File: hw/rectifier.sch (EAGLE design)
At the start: 0 parts

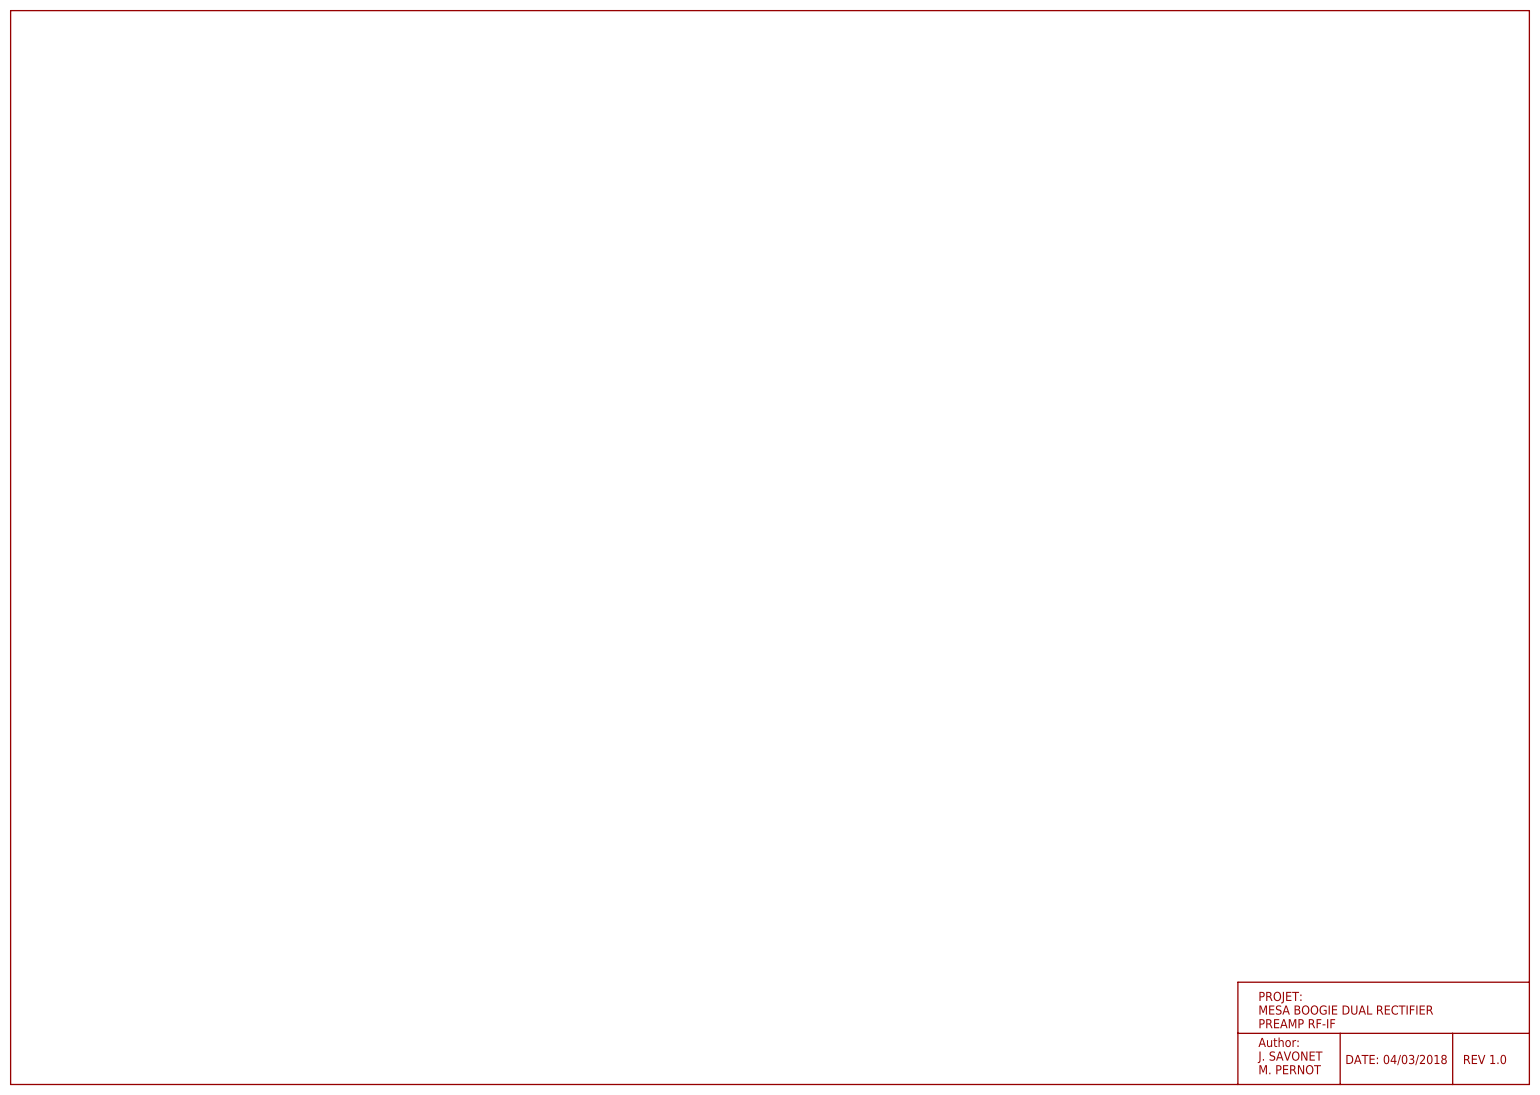
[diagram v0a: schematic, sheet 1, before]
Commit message: Add preamp
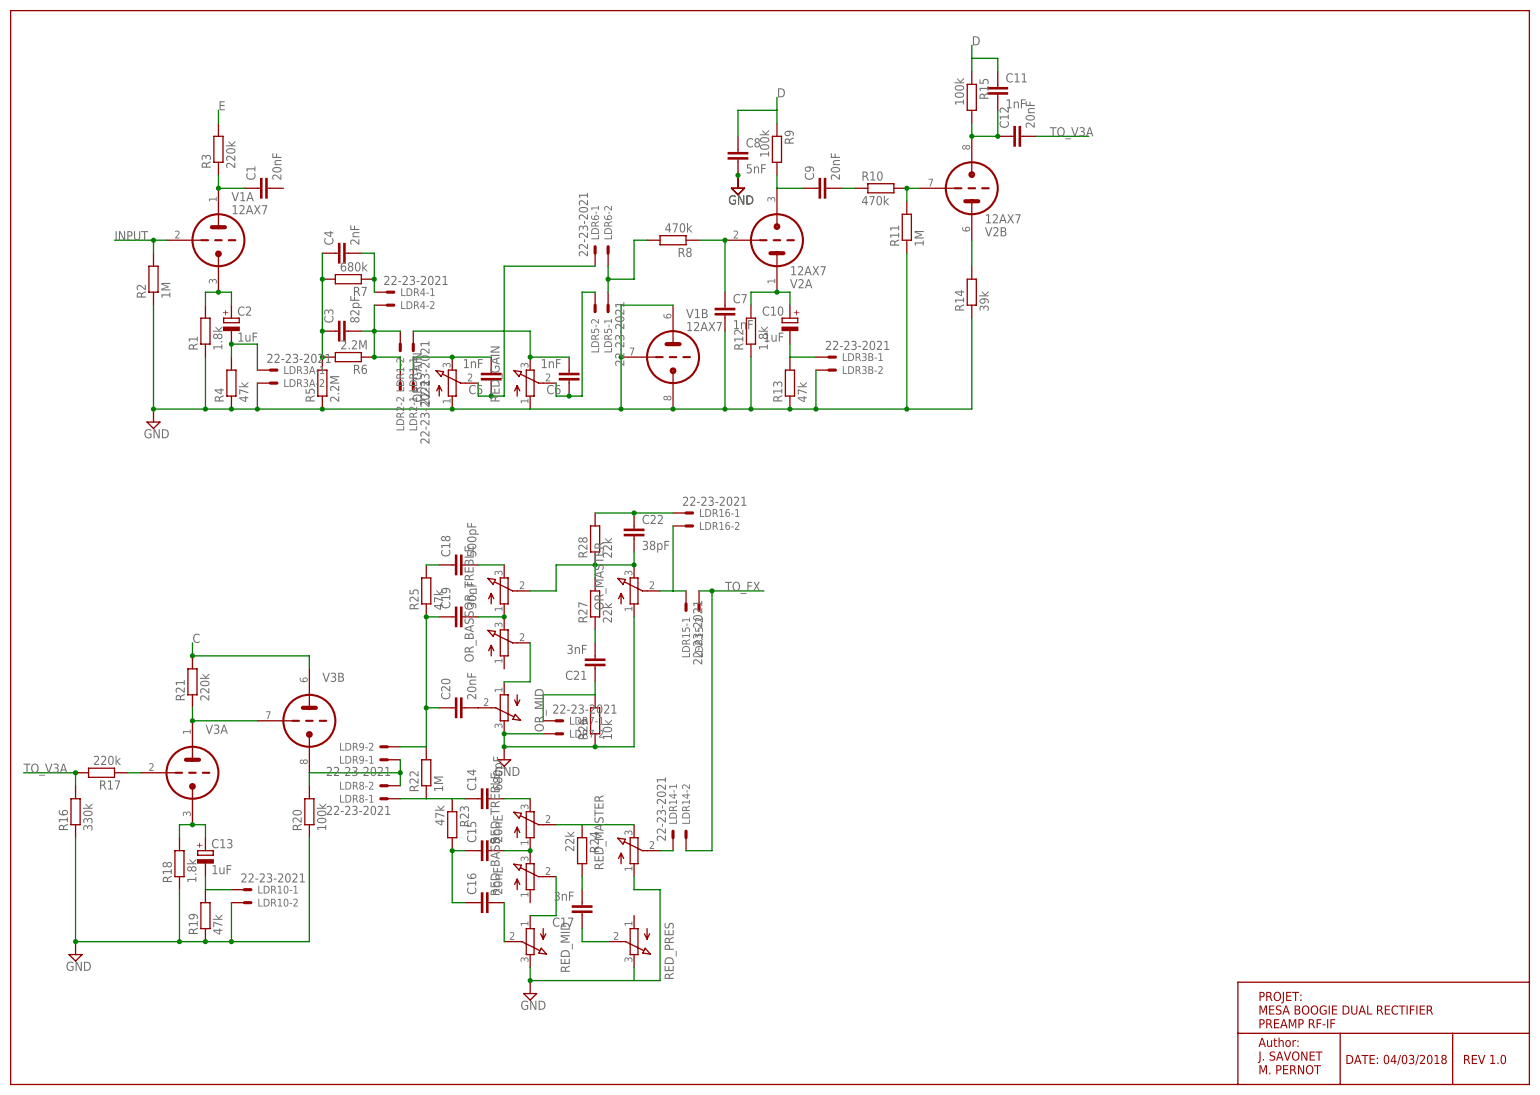
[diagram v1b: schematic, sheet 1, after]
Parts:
- added C1, C12, C15, C16, C20, C9: 20nF, capacitor-wima:C7.5/5
- added C10, C13, C2: 1uF, rcl:CPOL-EUE3.5-8
- added C11, C5, C6, C7: 1nF, capacitor-wima:C7.5/5
- added C14: 680pF, capacitor-wima:C7.5/5
- added C17, C21: 3nF, capacitor-wima:C7.5/5
- added C18: 500pF, capacitor-wima:C7.5/5
- added C19: 30nF, capacitor-wima:C7.5/5
- added C22: 38pF, capacitor-wima:C7.5/5
- added C3: 82pF, capacitor-wima:C7.5/5
- added C4: 2nF, capacitor-wima:C7.5/5
- added C8: 5nF, capacitor-wima:C7.5/5
- added LDR1, LDR10, LDR14, LDR15, LDR16, LDR2, LDR3A, LDR3B, LDR4, LDR5, LDR6, LDR7, LDR8, LDR9: 22-23-2021, con-molex:22-23-2021
- added OR_BASS, OR_GAIN, OR_MASTER, OR_MID, OR_TREBLE, RED_BASS, RED_GAIN, RED_MASTER, RED_MID, RED_PRES, RED_TREBLE: (no value), pot:3RP/1610N
- added R1, R12, R18: 1.8k, rcl:R-EU_0207/10
- added R10, R8: 470k, rcl:R-EU_0207/10
- added R11, R2, R22: 1M, rcl:R-EU_0207/10
- added R13, R19, R23, R25, R4: 47k, rcl:R-EU_0207/10
- added R14: 39k, rcl:R-EU_0207/10
- added R15, R20, R9: 100k, rcl:R-EU_0207/10
- added R16: 330k, rcl:R-EU_0207/10
- added R17, R21, R3: 220k, rcl:R-EU_0207/10
- added R24, R27, R28: 22k, rcl:R-EU_0207/10
- added R26: 10k, rcl:R-EU_0207/10
- added R5, R6: 2.2M, rcl:R-EU_0207/10
- added R7: 680k, rcl:R-EU_0207/10
- added V1, V2: 12AX7, tubes:12AX7-P
- added V3: (no value), tubes:12AX7-P
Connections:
- new net C: R21.2, V3B.TA
- new net D: C11.1, C8.1, R15.1, R9.1
- new net E: R3.2
- new net GND: C7.2, C8.2, LDR10-2.S, LDR3A-2.S, LDR3B-2.S, LDR7-2.S, OR_GAIN.A, OR_MASTER.A, OR_MID.E, R1.1, R11.1, R12.1, R13.1, R14.1, R16.1, R18.1, R19.1, R2.1, R20.1, R26.1, R4.1, R5.1, RED_GAIN.A, RED_MASTER.A, RED_MID.E, RED_PRES.E, V1B.TA, V1B.TG, V1B.TK
- new net INPUT: R2.2, V1A.TG
- new net LDR3_A: C2.-, LDR3A-1.S, R4.2
- new net LDR4_A: C4.2, LDR4-1.S, R7.1
- new net LDR4_B: C3.2, LDR1-2.S, LDR2-2.S, LDR4-2.S, R6.1
- new net N$1: C3.1, C4.1, R5.2, R6.2, R7.2
- new net N$10: C10.+, R12.2, V2A.TA
- new net N$11: C9.1, R9.2, V2A.TK
- new net N$12: R17.1, V3A.TG
- new net N$13: C10.-, LDR3B-1.S, R13.2
- new net N$14: C9.2, R10.1
- new net N$15: R10.2, R11.2, V2B.TG
- new net N$16: C13.+, R18.2, V3A.TK
- new net N$17: R14.2, V2B.TA
- new net N$18: C13.-, LDR10-1.S, R19.2
- new net N$19: C11.2, C12.1, R15.2, V2B.TK
- new net N$2: C2.+, R1.2, V1A.TK
- new net N$20: R21.1, V3A.TA, V3B.TG
- new net N$21: LDR8-2.S, LDR9-1.S, R20.2, V3B.TK
- new net N$22: C15.1, C16.1, R23.2
- new net N$23: C14.1, LDR8-1.S, R22.1, R23.1
- new net N$24: R24.1, RED_MASTER.E, RED_TREBLE.S
- new net N$25: C14.2, RED_TREBLE.E
- new net N$26: C15.2, RED_BASS.E, RED_TREBLE.A
- new net N$27: RED_BASS.S, RED_MID.A
- new net N$28: C16.2, RED_MID.S
- new net N$29: C19.1, C20.1, LDR9-2.S, R22.2, R25.1
- new net N$3: C1.1, R3.1, V1A.TA
- new net N$30: C17.2, R24.2
- new net N$31: C17.1, RED_PRES.S
- new net N$32: LDR14-1.S, RED_MASTER.S
- new net N$33: C18.1, R25.2
- new net N$34: C18.2, OR_TREBLE.E
- new net N$35: C19.2, OR_BASS.E, OR_TREBLE.A
- new net N$36: C20.2, OR_MID.S
- new net N$37: OR_BASS.S, OR_MID.A
- new net N$38: C21.1, LDR7-1.S, R26.2
- new net N$39: C21.2, R27.1
- new net N$4: LDR5-1.S, LDR6-2.S, R8.2
- new net N$40: C22.2, OR_MASTER.E, OR_TREBLE.S, R27.2, R28.1
- new net N$41: C22.1, LDR16-1.S, R28.2
- new net N$42: LDR15-1.S, LDR16-2.S, OR_MASTER.S
- new net N$5: C5.2, LDR2-1.S, OR_GAIN.E
- new net N$6: C5.1, LDR6-1.S, OR_GAIN.S
- new net N$7: C6.2, LDR1-1.S, RED_GAIN.E
- new net N$8: C6.1, LDR5-2.S, RED_GAIN.S
- new net N$9: C7.1, R8.1, V2A.TG
- new net TO_FX: LDR14-2.S, LDR15-2.S
- new net TO_V3A: C12.2, R16.2, R17.2

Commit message: Add loop section: wip
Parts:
- added C23, C28: 100nF, capacitor-wima:C7.5/5
- added C24: 47nF, capacitor-wima:C7.5/5
- added C27: 2u2, rcl:CPOL-EUE3.5-8
- added LDR3A1, LDR3A2, LDR3A3: 22-23-2021, con-molex:22-23-2021
- added LOOP_ACTIVE_MASTER, SEND_LEVEL: (no value), pot:3RP/1610N
- added R29, R30: 2M2, rcl:R-EU_0207/10
- added R31: 22k, rcl:R-EU_0207/10
- added R32: 82k, rcl:R-EU_0207/10
- added R33, R36: 1M, rcl:R-EU_0207/10
- added R34: 47k, rcl:R-EU_0207/10
- added R35: 2k2, rcl:R-EU_0207/10
- added R37: 120k, rcl:R-EU_0207/10
- added R38, R39: 3k3, rcl:R-EU_0207/10
- added V4: (no value), tubes:12AX7-P
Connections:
- new net N$43: C28.2, R29.1, R30.2, V4A.TG
- new net N$44: LDR3A1-2.S, LDR3A2-2.S, R34.2, V4B.TG
- new net N$45: R31.2, V4A.TK
- new net N$46: C23.1, R31.1, R32.2
- new net N$47: C23.2, LDR3A3-1.S, R33.2, R38.2, SEND_LEVEL.E
- new net N$48: C27.+, R35.2, V4B.TK
- new net N$49: C24.1, R37.1, V4B.TA
- new net N$50: LDR3A2-1.S, R38.1
- new net N$51: C24.2, LOOP_ACTIVE_MASTER.E
- new net N$52: LDR3A1-1.S, R39.1
- net C: now also R29.2, R37.2, V4A.TA
- net GND: now also C27.-, LOOP_ACTIVE_MASTER.A, R30.1, R32.1, R33.1, R34.1, R35.1, R36.1, SEND_LEVEL.A
- net TO_FX: now also C28.1, R36.2

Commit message: Start power section
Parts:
- added C26, C32, C33, C34: 30uF, rcl:CPOL-EUE3.5-8
- added C29: 047uF, capacitor-wima:C7.5/5
- added C30, C31: 220uF, rcl:CPOL-EUE3.5-8
- added D1, D2, D3, D4: 1N4004, diode:1N4004
- added L1: (no value), inductor-neosid:U15-CHOKE
- added LDR3: 22-23-2021, con-molex:22-23-2021
- added R41: 27k, rcl:R-EU_0207/10
- added R42, R43: 150k, rcl:R-EU_0207/10
- added R44: 2k7, rcl:R-EU_0207/10
- added R45: 15k, rcl:R-EU_0207/10
- added RECT_SELECT: 9077-2, switch-misc:9077-2
- added V5, V6: (no value), tubes:5U4GB
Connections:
- new net A: C29.2, L1.1, LDR3-2.S
- new net B: C26.+, L1.4, R44.1
- new net N$53: D1.C, D2.A
- new net N$54: D3.C, D4.A
- new net N$56: C30.-, C31.+, R42.2, R43.1
- new net N$57: V5.H1, V6.H1
- new net N$58: RECT_SELECT2.S, V5.A1, V6.A1
- new net N$59: RECT_SELECT1.S, V5.A2, V6.A2
- new net N$60: D3.A, RECT_SELECT2.O
- new net N$61: D1.A, RECT_SELECT1.O
- new net N$63: C30.+, D2.C, D4.C, LDR3-1.S, R42.1, V5.H2, V6.H2
- net C: now also C32.+, R41.2, R44.2, R45.2
- net D: now also C33.+, R45.1
- net E: now also C34.+, R41.1
- net GND: now also C26.-, C29.1, C31.-, C32.-, C33.-, C34.-, R43.2

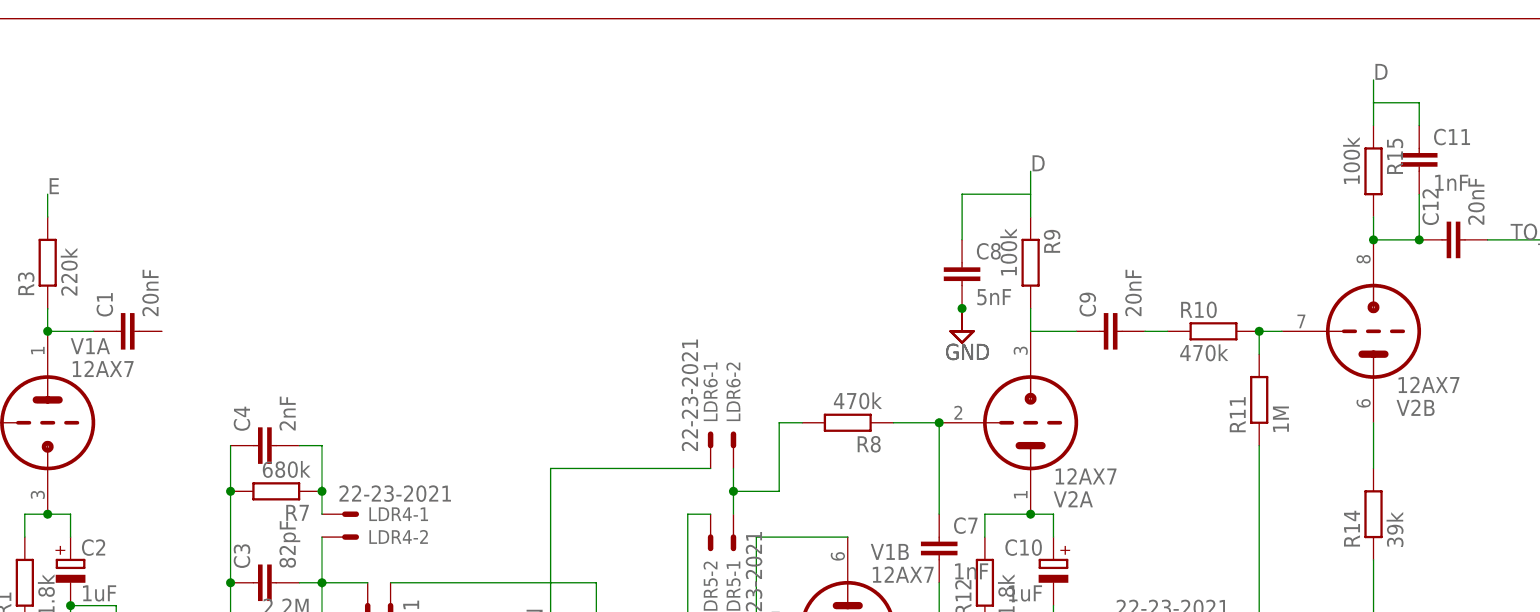
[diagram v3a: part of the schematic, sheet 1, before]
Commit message: Preamp: add missing wires
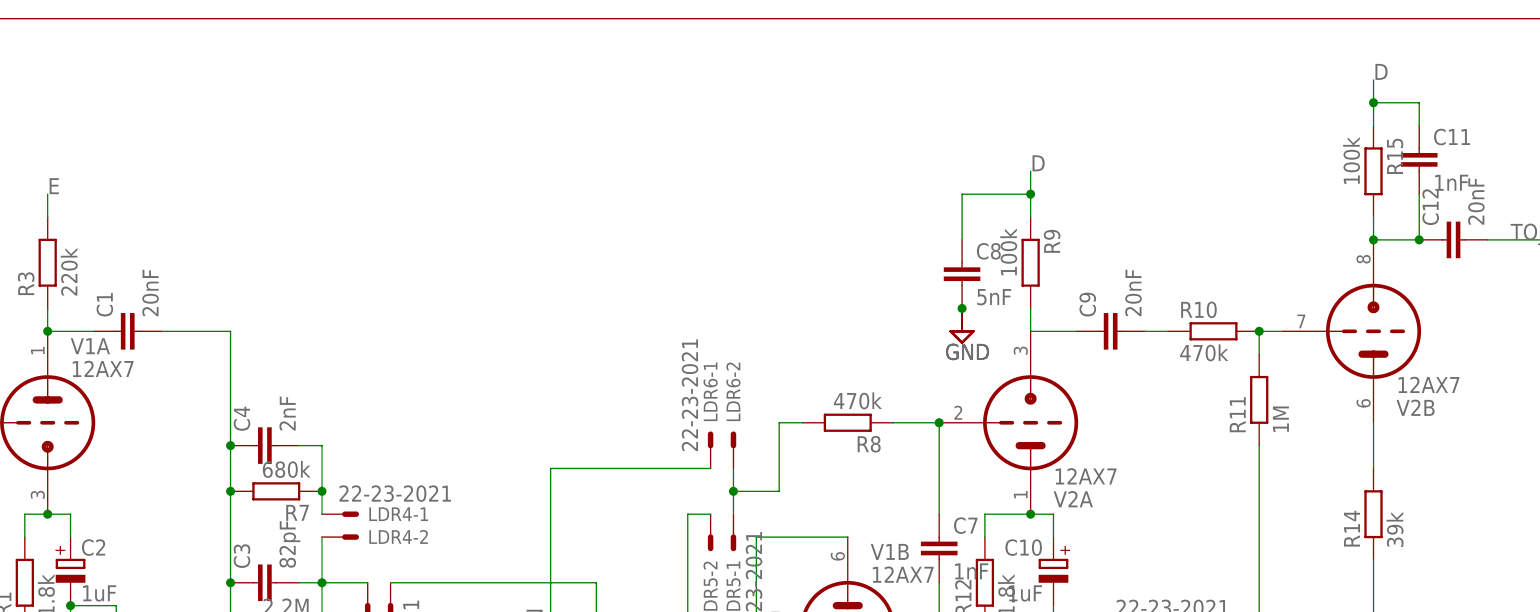
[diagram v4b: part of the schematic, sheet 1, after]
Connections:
- net N$1: now also C1.2
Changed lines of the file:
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@@
 <junction x="60.96" y="147.32"/>
 <junction x="60.96" y="142.24"/>
+<pinref part="C1" gate="G$1" pin="2"/>
+<wire x1="53.34" y1="175.26" x2="60.96" y2="175.26" width="0.1524" layer="91"/>
+<wire x1="60.96" y1="175.26" x2="60.96" y2="162.56" width="0.1524" layer="91"/>
+<junction x="60.96" y="162.56"/>
 </segment>
 </net>
@@
 <wire x1="149.86" y1="190.5" x2="149.86" y2="193.04" width="0.1524" layer="91"/>
 <label x="149.86" y="193.04" size="1.778" layer="95"/>
+<junction x="149.86" y="190.5"/>
 </segment>
 <segment>
@@
 <wire x1="187.96" y1="200.66" x2="187.96" y2="203.2" width="0.1524" layer="91"/>
 <label x="187.96" y="203.2" size="1.778" layer="95"/>
+<junction x="187.96" y="200.66"/>
 </segment>
 </net>
